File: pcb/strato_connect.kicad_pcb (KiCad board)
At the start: 4 copper layers, 38.6 x 40.3 mm, 49 parts, among them J1 Conn_Coaxial, J2 Conn_01x04_Pin, J3 Conn_01x04_Pin, J5 Conn_01x01_Pin, J6 Conn_01x02_Pin, SW1 SW_SPST, U1 TPS565242, U2 ATmega328PB-M, U4 RF4463F30, Y1 CSTNE16M0V530000R0

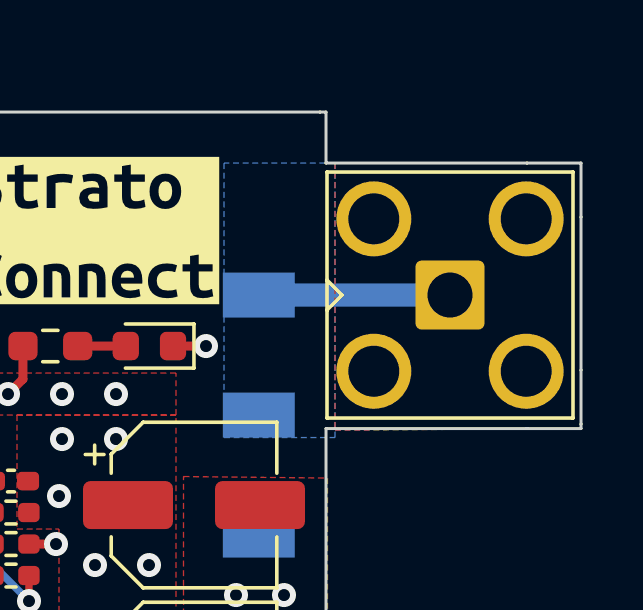
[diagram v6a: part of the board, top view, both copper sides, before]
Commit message: Switch the coax connector type
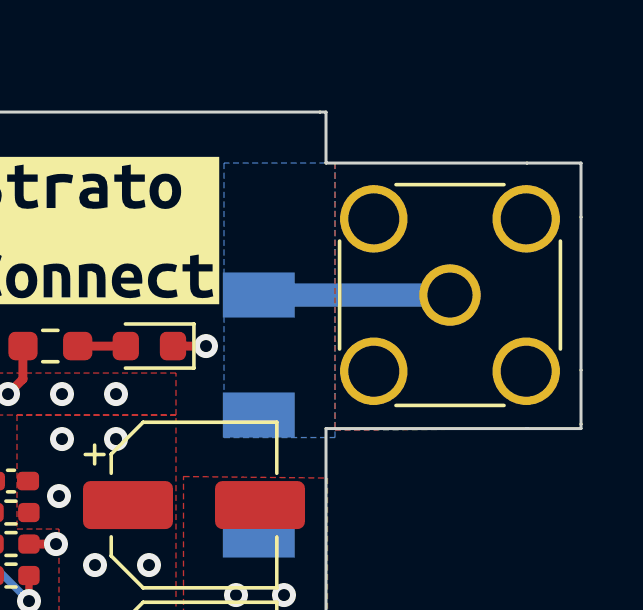
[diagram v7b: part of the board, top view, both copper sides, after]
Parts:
- J1: footprint Connector_Coaxial:SMA_Amphenol_901-143_Horizontal -> Connector_Coaxial:SMA_Wurth_60312002114503_Vertical
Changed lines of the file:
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@@
   (net 46 "unconnected-(U4-NC-Pad14)")
   (net 47 "unconnected-(J2-Pin_3-Pad3)")
-  (footprint "Connector_Coaxial:SMA_Amphenol_901-143_Horizontal" (layer "F.Cu")
+  (footprint "Connector_Coaxial:SMA_Wurth_60312002114503_Vertical" (layer "F.Cu")
     (at 175.133 63.8)
-    (descr " Amphenol RF 901-143 https://www.amphenolrf.com/library/download/link/link_id/585682")
-    (tags "SMA THT Female Jack Horizontal")
+    (descr "https://www.we-online.de/katalog/datasheet/60312002114503.pdf")
+    (tags "SMA THT Female Jack Vertical ExtendedLegs")
     (property "Sheetfile" "strato_connect.kicad_sch")
     (property "Sheetname" "")
@@
     (property "ki_keywords" "BNC SMA SMB SMC LEMO coaxial connector CINCH RCA")
     (attr through_hole)
-    (fp_text reference "J1" (at -5.2 0 90) (layer "F.SilkS") hide
+    (fp_text reference "J1" (at 0 -4.75) (layer "F.SilkS") hide
         (effects (font (size 1 1) (thickness 0.15)))
     )
-    (fp_text value "Conn_Coaxial" (at 0 5) (layer "F.Fab") hide
+    (fp_text value "Conn_Coaxial" (at 0 5) (layer "F.Fab")
         (effects (font (size 1 1) (thickness 0.15)))
     )
@@
         (effects (font (size 1 1) (thickness 0.15)))
     )
-    (fp_line (start -4.1 -4.1) (end -4.1 4.1)
+    (fp_line (start -3.68 -1.8) (end -3.68 1.8)
       (stroke (width 0.12) (type solid)) (layer "F.SilkS"))
-    (fp_line (start -4.1 -4.1) (end 4.1 -4.1)
+    (fp_line (start -1.8 -3.68) (end 1.8 -3.68)
       (stroke (width 0.12) (type solid)) (layer "F.SilkS"))
-    (fp_line (start -4.1 0.5) (end -3.6 0)
+    (fp_line (start -1.8 3.68) (end 1.8 3.68)
       (stroke (width 0.12) (type solid)) (layer "F.SilkS"))
-    (fp_line (start -4.1 4.1) (end 4.1 4.1)
+    (fp_line (start 3.68 -1.8) (end 3.68 1.8)
       (stroke (width 0.12) (type solid)) (layer "F.SilkS"))
-    (fp_line (start -3.6 0) (end -4.1 -0.5)
-      (stroke (width 0.12) (type solid)) (layer "F.SilkS"))
-    (fp_line (start 4.1 -4.1) (end 4.1 4.1)
-      (stroke (width 0.12) (type solid)) (layer "F.SilkS"))
-    (fp_line (start -4.3 -12) (end -4.3 4.3)
+    (fp_line (start -4.17 -4.17) (end -4.17 4.17)
       (stroke (width 0.05) (type solid)) (layer "F.CrtYd"))
-    (fp_line (start -4.3 -12) (end 4.3 -12)
+    (fp_line (start -4.17 -4.17) (end 4.17 -4.17)
       (stroke (width 0.05) (type solid)) (layer "F.CrtYd"))
-    (fp_line (start 4.3 4.3) (end -4.3 4.3)
+    (fp_line (start 4.17 4.17) (end -4.17 4.17)
       (stroke (width 0.05) (type solid)) (layer "F.CrtYd"))
-    (fp_line (start 4.3 4.3) (end 4.3 -12)
+    (fp_line (start 4.17 4.17) (end 4.17 -4.17)
       (stroke (width 0.05) (type solid)) (layer "F.CrtYd"))
     (fp_line (start -3.5 -3.5) (end -3.5 3.5)
@@
     (fp_line (start -3.5 -3.5) (end 3.5 -3.5)
       (stroke (width 0.1) (type solid)) (layer "F.Fab"))
-    (fp_line (start -3.5 -1) (end -2.5 0)
-      (stroke (width 0.1) (type solid)) (layer "F.Fab"))
     (fp_line (start -3.5 3.5) (end 3.5 3.5)
       (stroke (width 0.1) (type solid)) (layer "F.Fab"))
-    (fp_line (start -3 -9.5) (end 3 -10)
-      (stroke (width 0.1) (type solid)) (layer "F.Fab"))
-    (fp_line (start -3 -9) (end 3 -9.5)
-      (stroke (width 0.1) (type solid)) (layer "F.Fab"))
-    (fp_line (start -3 -8.5) (end 3 -9)
-      (stroke (width 0.1) (type solid)) (layer "F.Fab"))
-    (fp_line (start -3 -8) (end 3 -8.5)
-      (stroke (width 0.1) (type solid)) (layer "F.Fab"))
-    (fp_line (start -3 -7.5) (end 3 -8)
-      (stroke (width 0.1) (type solid)) (layer "F.Fab"))
-    (fp_line (start -3 -7) (end 3 -7.5)
-      (stroke (width 0.1) (type solid)) (layer "F.Fab"))
-    (fp_line (start -3 -5.5) (end -3 -3.5)
-      (stroke (width 0.1) (type solid)) (layer "F.Fab"))
-    (fp_line (start -2.5 -11.5) (end -2.5 -5.5)
-      (stroke (width 0.1) (type solid)) (layer "F.Fab"))
-    (fp_line (start -2.5 -11.5) (end 2.5 -11.5)
-      (stroke (width 0.1) (type solid)) (layer "F.Fab"))
-    (fp_line (start -2.5 0) (end -3.5 1)
-      (stroke (width 0.1) (type solid)) (layer "F.Fab"))
-    (fp_line (start 2.5 -11.5) (end 2.5 -5.5)
-      (stroke (width 0.1) (type solid)) (layer "F.Fab"))
-    (fp_line (start 3 -5.5) (end -3 -5.5)
-      (stroke (width 0.1) (type solid)) (layer "F.Fab"))
-    (fp_line (start 3 -5.5) (end 3 -3.5)
-      (stroke (width 0.1) (type solid)) (layer "F.Fab"))
     (fp_line (start 3.5 -3.5) (end 3.5 3.5)
       (stroke (width 0.1) (type solid)) (layer "F.Fab"))
-    (pad "1" thru_hole roundrect (at 0 0) (size 2.3 2.3) (drill 1.5) (layers "*.Cu" "*.Mask") (remove_unused_layers) (keep_end_layers) (zone_layer_connections) (roundrect_rratio 0.087)
+    (fp_circle (center 0 0) (end 3.175 0)
+      (stroke (width 0.1) (type solid)) (fill none) (layer "F.Fab"))
+    (pad "1" thru_hole circle (at 0 0) (size 2.05 2.05) (drill 1.5) (layers "*.Cu" "*.Mask")
       (net 10 "Net-(J1-In)") (pinfunction "In") (pintype "passive"))
-    (pad "2" thru_hole circle (at -2.54 -2.54) (size 2.5 2.5) (drill 1.7) (layers "*.Cu" "*.Mask") (remove_unused_layers) (keep_end_layers) (zone_layer_connections "In1.Cu" "In2.Cu")
+    (pad "2" thru_hole circle (at -2.54 -2.54) (size 2.25 2.25) (drill 1.7) (layers "*.Cu" "*.Mask")
       (net 11 "/RF_GND") (pinfunction "Ext") (pintype "passive"))
-    (pad "2" thru_hole circle (at -2.54 2.54) (size 2.5 2.5) (drill 1.7) (layers "*.Cu" "*.Mask") (remove_unused_layers) (keep_end_layers) (zone_layer_connections "In1.Cu" "In2.Cu")
+    (pad "2" thru_hole circle (at -2.54 2.54) (size 2.25 2.25) (drill 1.7) (layers "*.Cu" "*.Mask")
       (net 11 "/RF_GND") (pinfunction "Ext") (pintype "passive"))
-    (pad "2" thru_hole circle (at 2.54 -2.54) (size 2.5 2.5) (drill 1.7) (layers "*.Cu" "*.Mask") (remove_unused_layers) (keep_end_layers) (zone_layer_connections "In1.Cu" "In2.Cu")
+    (pad "2" thru_hole circle (at 2.54 -2.54) (size 2.25 2.25) (drill 1.7) (layers "*.Cu" "*.Mask")
       (net 11 "/RF_GND") (pinfunction "Ext") (pintype "passive"))
-    (pad "2" thru_hole circle (at 2.54 2.54) (size 2.5 2.5) (drill 1.7) (layers "*.Cu" "*.Mask") (remove_unused_layers) (keep_end_layers) (zone_layer_connections "In1.Cu" "In2.Cu")
+    (pad "2" thru_hole circle (at 2.54 2.54) (size 2.25 2.25) (drill 1.7) (layers "*.Cu" "*.Mask")
       (net 11 "/RF_GND") (pinfunction "Ext") (pintype "passive"))
-    (model "${KICAD6_3DMODEL_DIR}/Connector_Coaxial.3dshapes/SMA_Amphenol_901-143_Horizontal.wrl"
+    (model "${KICAD6_3DMODEL_DIR}/Connector_Coaxial.3dshapes/SMA_Wurth_60312002114503_Vertical.wrl"
       (offset (xyz 0 0 0))
       (scale (xyz 1 1 1))
@@
     (attr board_only exclude_from_pos_files exclude_from_bom)
     (fp_text reference "kibuzzard-64B1A895" (at 0 -3.983434) (layer "F.SilkS") hide
-        (effects (font (size 0 0)))
+        (effects (font (size 0 0) (thickness 0.15)))
     )
     (fp_text value "G***" (at 0 3.983434) (layer "F.SilkS") hide
-        (effects (font (size 0 0)))
+        (effects (font (size 0 0) (thickness 0.15)))
     )
     (fp_poly
@@
     (attr board_only exclude_from_pos_files exclude_from_bom)
     (fp_text reference "kibuzzard-64B1B6FD" (at 0 -3.803015) (layer "F.SilkS") hide
-        (effects (font (size 0 0)))
+        (effects (font (size 0 0) (thickness 0.15)))
     )
     (fp_text value "G***" (at 0 3.803015) (layer "F.SilkS") hide
-        (effects (font (size 0 0)))
+        (effects (font (size 0 0) (thickness 0.15)))
     )
     (fp_poly
@@
     (attr board_only exclude_from_pos_files exclude_from_bom)
     (fp_text reference "kibuzzard-64B1A828" (at 0 -4.007247) (layer "F.SilkS") hide
-        (effects (font (size 0 0)))
+        (effects (font (size 0 0) (thickness 0.15)))
     )
     (fp_text value "G***" (at 0 4.007247) (layer "F.SilkS") hide
-        (effects (font (size 0 0)))
+        (effects (font (size 0 0) (thickness 0.15)))
     )
     (fp_poly
@@
     (attr board_only exclude_from_pos_files exclude_from_bom)
     (fp_text reference "kibuzzard-64B1A87B" (at 0 -4.015581) (layer "F.SilkS") hide
-        (effects (font (size 0 0)))
+        (effects (font (size 0 0) (thickness 0.15)))
     )
     (fp_text value "G***" (at 0 4.015581) (layer "F.SilkS") hide
-        (effects (font (size 0 0)))
+        (effects (font (size 0 0) (thickness 0.15)))
     )
     (fp_poly
@@
     (attr board_only exclude_from_pos_files exclude_from_bom)
     (fp_text reference "kibuzzard-64B1B5E1" (at 0 -5.503634) (layer "F.SilkS") hide
-        (effects (font (size 0 0)))
+        (effects (font (size 0 0) (thickness 0.15)))
     )
     (fp_text value "G***" (at 0 5.503634) (layer "F.SilkS") hide
-        (effects (font (size 0 0)))
+        (effects (font (size 0 0) (thickness 0.15)))
     )
     (fp_poly
@@
         (xy 157.8 67.8)
         (xy 160.7 67.8)
-        (xy 160.7 67.8)
         (xy 166 67.8)
         (xy 166 66.4)
@@
         (xy 156.8 72.4)
         (xy 156.8 72)
-        (xy 156.8 72)
-        (xy 156.8 69.9)
         (xy 156.8 69.9)
         (xy 156.8 68.1)

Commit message: WIP
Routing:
- net UART_RX: track 8.77 -> 12.5 mm
- net SPI_MOSI: track 20.8 -> 23.1 mm
- net GND: track 21.4 -> 22.7 mm, vias 23 -> 24
- net (no net): vias 1 -> 0
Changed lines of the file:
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@@
     (effects (font (size 1.5 1.5) (thickness 0.3) bold) (justify left bottom))
   )
-  (via (at 166.15 94.35) (size 0.8) (drill 0.4) (layers "F.Cu" "B.Cu") (net 0))
   (segment (start 159.6375 82.8375) (end 160.3 83.5) (width 0.25) (layer "F.Cu") (net 1))
   (segment (start 158.9865 82.8375) (end 159.6375 82.8375) (width 0.25) (layer "F.Cu") (net 1))
@@
   (segment (start 154.1115 82.8375) (end 156.299 82.8375) (width 0.25) (layer "F.Cu") (net 2))
   (segment (start 157.5 70.6625) (end 157.5 71.4) (width 0.55) (layer "F.Cu") (net 2))
+  (segment (start 166.15 93.1) (end 166.15 94.35) (width 0.25) (layer "F.Cu") (net 2))
   (segment (start 158.641 88.684) (end 157.984 88.684) (width 0.25) (layer "F.Cu") (net 2))
   (segment (start 158.8465 69.8025) (end 158.8465 68.9465) (width 0.3) (layer "F.Cu") (net 2))
@@
   (segment (start 157.984 88.684) (end 157.7 88.4) (width 0.25) (layer "F.Cu") (net 2))
   (via (at 157.7 88.4) (size 0.8) (drill 0.4) (layers "F.Cu" "B.Cu") (free) (net 2))
+  (via (at 166.15 94.35) (size 0.8) (drill 0.4) (layers "F.Cu" "B.Cu") (free) (net 2))
   (via (at 162 72.1) (size 0.8) (drill 0.4) (layers "F.Cu" "B.Cu") (free) (net 2))
   (via (at 167 65.5) (size 0.8) (drill 0.4) (layers "F.Cu" "B.Cu") (free) (net 2))
@@
   (segment (start 157.815 76.8) (end 158.695 77.68) (width 0.25) (layer "F.Cu") (net 14))
   (segment (start 155.299 77.701) (end 155.3 77.7) (width 0.25) (layer "F.Cu") (net 14))
-  (segment (start 158.695 77.68) (end 158.695 78.387106) (width 0.25) (layer "B.Cu") (net 14))
-  (segment (start 158.695 78.387106) (end 168.107894 87.8) (width 0.25) (layer "B.Cu") (net 14))
+  (segment (start 158.695 77.68) (end 159.865 78.85) (width 0.25) (layer "B.Cu") (net 14))
+  (segment (start 165.25 85.45) (end 167.6 87.8) (width 0.25) (layer "B.Cu") (net 14))
+  (segment (start 159.865 78.85) (end 162.15 78.85) (width 0.25) (layer "B.Cu") (net 14))
+  (segment (start 167.6 87.8) (end 168.76 87.8) (width 0.25) (layer "B.Cu") (net 14))
+  (segment (start 165.25 81.95) (end 165.25 85.45) (width 0.25) (layer "B.Cu") (net 14))
+  (segment (start 162.15 78.85) (end 165.25 81.95) (width 0.25) (layer "B.Cu") (net 14))
   (segment (start 156.9 86.1) (end 157.922 87.122) (width 0.25) (layer "F.Cu") (net 15))
   (segment (start 168.15 91.85) (end 164 87.7) (width 0.25) (layer "F.Cu") (net 15))
@@
   (segment (start 160.2675 86.27) (end 161.1 87.1025) (width 0.25) (layer "F.Cu") (net 16))
   (segment (start 157.3 85.299376) (end 157.3 85.51) (width 0.25) (layer "F.Cu") (net 16))
+  (segment (start 161.1 88.625) (end 161.6 89.125) (width 0.25) (layer "F.Cu") (net 17))
+  (segment (start 165.3 95.25) (end 166.8 95.25) (width 0.25) (layer "F.Cu") (net 17))
+  (segment (start 167.15 94.9) (end 167.15 93.1) (width 0.25) (layer "F.Cu") (net 17))
+  (segment (start 164.425 94.375) (end 165.3 95.25) (width 0.25) (layer "F.Cu") (net 17))
   (segment (start 164.425 93.609619) (end 164.425 94.375) (width 0.25) (layer "F.Cu") (net 17))
-  (segment (start 167.05 94.375) (end 167.15 94.275) (width 0.25) (layer "F.Cu") (net 17))
+  (segment (start 161.6 89.125) (end 161.6 90.784619) (width 0.25) (layer "F.Cu") (net 17))
+  (segment (start 166.8 95.25) (end 167.15 94.9) (width 0.25) (layer "F.Cu") (net 17))
+  (segment (start 161.1 88.2975) (end 161.1 88.625) (width 0.25) (layer "F.Cu") (net 17))
   (segment (start 161.6 90.784619) (end 164.425 93.609619) (width 0.25) (layer "F.Cu") (net 17))
-  (segment (start 161.1 88.2975) (end 161.1 88.625) (width 0.25) (layer "F.Cu") (net 17))
-  (segment (start 161.1 88.625) (end 161.6 89.125) (width 0.25) (layer "F.Cu") (net 17))
-  (segment (start 161.6 89.125) (end 161.6 90.784619) (width 0.25) (layer "F.Cu") (net 17))
-  (segment (start 167.15 94.275) (end 167.15 93.1) (width 0.25) (layer "F.Cu") (net 17))
   (segment (start 157.799 85.025) (end 157.799 85.449) (width 0.25) (layer "F.Cu") (net 18))
   (segment (start 157.799 85.449) (end 158.25 85.9) (width 0.25) (layer "F.Cu") (net 18))
